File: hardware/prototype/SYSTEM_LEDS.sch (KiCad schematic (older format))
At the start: 9 parts, among them Q1 DTC143Z

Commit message: Complete PCB layout
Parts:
- renumbered D1 to D3, D2 to D4, D19 to D5, D20 to D6, Q1 to Q2, R2 to R8, R6 to R9
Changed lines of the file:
@@
 	1350 4000 1450 4000
 $Comp
-L Device:R R2
+L Device:R R8
 U 1 1 5AE81518
 P 1800 3500
-F 0 "R2" H 1700 3500 50  0000 C CNN
+F 0 "R8" H 1700 3500 50  0000 C CNN
 F 1 "110R" V 1800 3500 50  0000 C CNN
 F 2 "Resistor_SMD:R_0805_2012Metric" V 1730 3500 50  0001 C CNN
@@
 $EndComp
 $Comp
-L power:GND #PWR0101
+L power:GND #PWR041
 U 1 1 5AE8151F
 P 1800 4210
-F 0 "#PWR0101" H 1800 3960 50  0001 C CNN
+F 0 "#PWR041" H 1800 3960 50  0001 C CNN
 F 1 "GND" H 1925 4135 50  0000 C CNN
 F 2 "" H 1800 4210 50  0001 C CNN
@@
 GPS FIX indicator
 $Comp
-L Transistor_BJT:DTC143Z Q1
+L Transistor_BJT:DTC143Z Q2
 U 1 1 5AE81531
 P 1700 4000
-F 0 "Q1" H 1888 4046 50  0000 L CNN
+F 0 "Q2" H 1888 4046 50  0000 L CNN
 F 1 "DTC143Z" H 1888 3955 50  0000 L CNN
 F 2 "Package_TO_SOT_SMD:SC-59_Handsoldering" H 1700 4000 50  0001 L CNN
@@
 	8850 3600 8850 3250
 $Comp
-L power:GND #PWR0102
+L power:GND #PWR043
 U 1 1 5AEBED95
 P 8850 4000
-F 0 "#PWR0102" H 8850 3750 50  0001 C CNN
+F 0 "#PWR043" H 8850 3750 50  0001 C CNN
 F 1 "GND" H 9000 3900 50  0000 C CNN
 F 2 "" H 8850 4000 50  0001 C CNN
@@
 GLOBAL_3V3
 $Comp
-L Device:LED D20
+L Device:LED D6
 U 1 1 5AEBF85D
 P 10650 3100
-F 0 "D20" V 10550 3000 50  0000 R CNN
+F 0 "D6" V 10550 3000 50  0000 R CNN
 F 1 "LED" V 10650 3000 50  0000 R CNN
 F 2 "LED_SMD:LED_0805_2012Metric_Pad0.97x1.50mm_HandSolder" H 10650 3100 50  0001 C CNN
@@
 	10650 3600 10650 3250
 $Comp
-L power:GND #PWR0103
+L power:GND #PWR044
 U 1 1 5AEBF86D
 P 10650 4000
-F 0 "#PWR0103" H 10650 3750 50  0001 C CNN
+F 0 "#PWR044" H 10650 3750 50  0001 C CNN
 F 1 "GND" H 10800 3900 50  0000 C CNN
 F 2 "" H 10650 4000 50  0001 C CNN
@@
 5v power indicator
 $Comp
-L Device:LED D2
+L Device:LED D4
 U 1 1 5AEC051D
 P 5600 3200
-F 0 "D2" V 5550 3100 50  0000 R CNN
+F 0 "D4" V 5550 3100 50  0000 R CNN
 F 1 "LED" V 5650 3100 50  0000 R CNN
 F 2 "LED_SMD:LED_0805_2012Metric_Pad0.97x1.50mm_HandSolder" H 5600 3200 50  0001 C CNN
@@
 	5600 3050 5350 3050
 $Comp
-L Device:R R6
+L Device:R R9
 U 1 1 5AEC0525
 P 5600 3850
-F 0 "R6" H 5700 3850 50  0000 C CNN
+F 0 "R9" H 5700 3850 50  0000 C CNN
 F 1 "130R" V 5600 3850 50  0000 C CNN
 F 2 "Resistor_SMD:R_0805_2012Metric" V 5530 3850 50  0001 C CNN
@@
 	5600 3700 5600 3350
 $Comp
-L power:GND #PWR0104
+L power:GND #PWR042
 U 1 1 5AEC052D
 P 5600 4100
-F 0 "#PWR0104" H 5600 3850 50  0001 C CNN
+F 0 "#PWR042" H 5600 3850 50  0001 C CNN
 F 1 "GND" H 5750 4000 50  0000 C CNN
 F 2 "" H 5600 4100 50  0001 C CNN
@@
 Red_LED
 $Comp
-L Device:LED D19
+L Device:LED D5
 U 1 1 5AEC1D57
 P 8850 3100
-F 0 "D19" V 8750 3000 50  0000 R CNN
+F 0 "D5" V 8750 3000 50  0000 R CNN
 F 1 "LED" V 8850 3000 50  0000 R CNN
 F 2 "LED_SMD:LED_0805_2012Metric_Pad0.97x1.50mm_HandSolder" H 8850 3100 50  0001 C CNN
@@
 $EndComp
 $Comp
-L Device:LED D1
+L Device:LED D3
 U 1 1 5B00BAB6
 P 1800 3100
-F 0 "D1" V 1700 3000 50  0000 R CNN
+F 0 "D3" V 1700 3000 50  0000 R CNN
 F 1 "LED" V 1800 3000 50  0000 R CNN
 F 2 "LED_SMD:LED_0805_2012Metric_Pad0.97x1.50mm_HandSolder" H 1800 3100 50  0001 C CNN

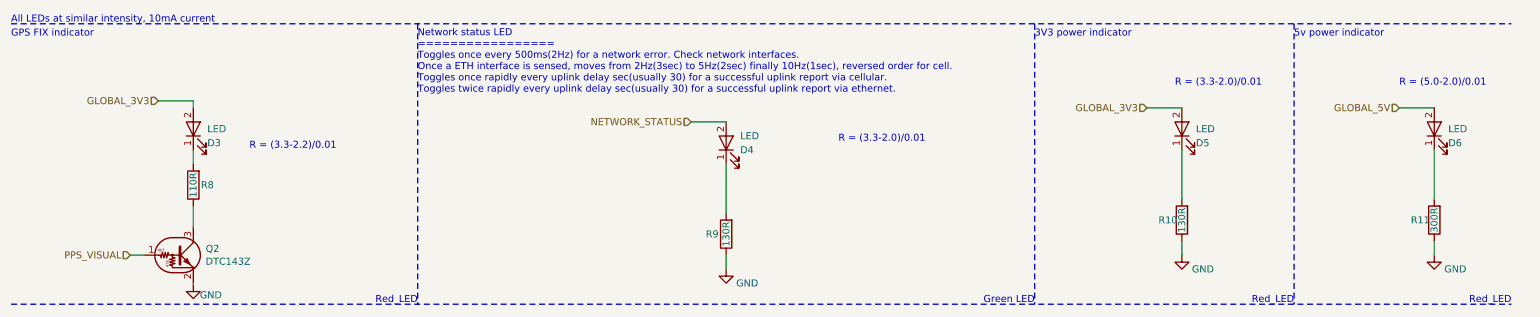
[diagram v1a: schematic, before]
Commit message: Complete PCB design, BOM generation and gerber generation
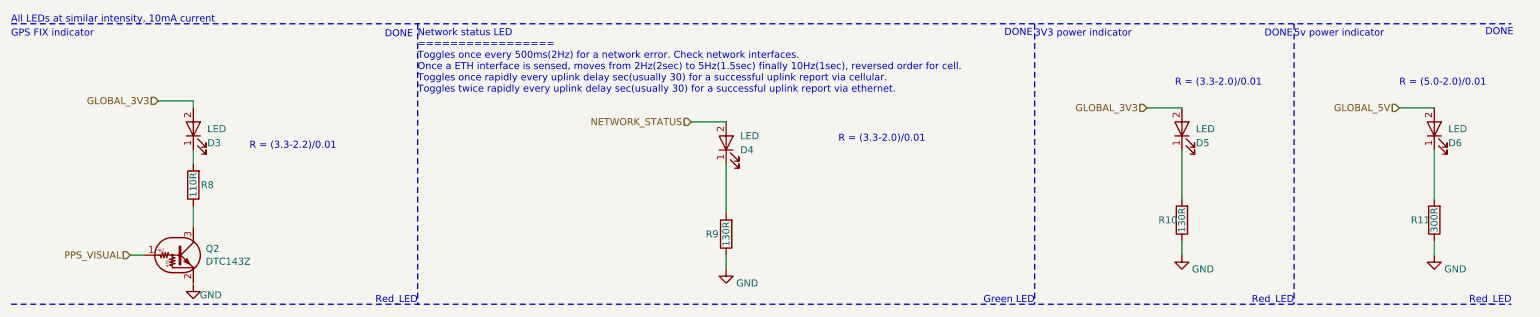
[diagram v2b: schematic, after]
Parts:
- D3, D5, D6: manf# (none) -> LTST-C171KRKT
- D4: manf# (none) -> LTST-C171KGKT
- Q2: manf# (none) -> DTC143ZKAT146
- R10, R9: manf# (none) -> ERA-6AEB131V; purchase_page (none) -> https://www.digikey.com/product-detail/en/panasonic-electro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
- R11: manf# (none) -> ERJ-PB6D3000V; purchase_page (none) -> https://www.digikey.com/product-detail/en/panasonic-electro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
- R8: manf# (none) -> CRCW0805110RFKEA; purchase_page (none) -> https://www.digikey.com/product-detail/en/vishay-dale/CRCW0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
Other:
- note added: "DONE"
- note added: "Network status LED\n=================\nToggles once every 500ms(2Hz) for a network error. Check network interfaces.\nOnce a ETH interface is sensed, moves from 2Hz(2sec) to 5Hz(1.5sec) finally 10Hz(1sec), reversed order for cell.\nToggles once rapidly every uplink delay sec(usually 30) for a successful uplink report via cellular.\nToggles twice rapidly every uplink delay sec(usually 30) for a suc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"
- note removed: "Network status LED\n=================\nToggles once every 500ms(2Hz) for a network error. Check network interfaces.\nOnce a ETH interface is sensed, moves from 2Hz(3sec) to 5Hz(2sec) finally 10Hz(1sec), reversed order for cell.\nToggles once rapidly every uplink delay sec(usually 30) for a successful uplink report via cellular.\nToggles twice rapidly every uplink delay sec(usually 30) for a succe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"
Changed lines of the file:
@@
 $Descr A4 11693 8268
 encoding utf-8
-Sheet 2 2
-Title ""
-Date ""
-Rev ""
-Comp ""
-Comment1 ""
+Sheet 2 3
+Title "ESP32 LoRa gateway with surge suppression"
+Date "2018-04-30"
+Rev "1"
+Comp "Kaiote Limited"
+Comment1 "Design by: Alois Mbutura"
 Comment2 ""
 Comment3 ""
@@
 F 1 "110R" V 1800 3500 50  0000 C CNN
 F 2 "Resistor_SMD:R_0805_2012Metric" V 1730 3500 50  0001 C CNN
-F 3 "~" H 1800 3500 50  0001 C CNN
+F 3 "http://www.vishay.com/docs/20035/dcrcwe3.pdf" H 1800 3500 50  0001 C CNN
+F 4 "https://www.digikey.com/product-detail/en/vishay-dale/CRCW0805110RFKEA/541-110CCT-ND/1180673" H 1800 3500 50  0001 C CNN "purchase_page"
+F 5 "CRCW0805110RFKEA" H 1800 3500 50  0001 C CNN "manf#"
 	1    1800 3500
 	-1   0    0    1
@@
 F 3 "http://www.rohm.com/web/global/datasheet/DTC143ZEB/dtc143zebtl-e" H 1700 4000 50  0001 L CNN
 F 4 "https://www.digikey.com/product-detail/en/rohm-semiconductor/DTC143ZKAT146/DTC143ZKAT146CT-ND/650725" H 1700 4000 50  0001 C CNN "purchase page"
+F 5 "DTC143ZKAT146" H 1700 4000 50  0001 C CNN "manf#"
 	1    1700 4000
 	1    0    0    -1
@@
 GLOBAL_3V3
 Text Notes 3400 2850 0    50   ~ 0
-Network status LED\n=================\nToggles once every 500ms(2Hz) for a network error. Check network interfaces.\nOnce a ETH interface is sensed, moves from 2Hz(3sec) to 5Hz(2sec) finally 10Hz(1sec), reversed order for cell.\nToggles once rapidly every uplink delay sec(usually 30) for a successful uplink report via cellular.\nToggles twice rapidly every uplink delay sec(usually 30) for a successful uplink report via ethernet.
+Network status LED\n=================\nToggles once every 500ms(2Hz) for a network error. Check network interfaces.\nOnce a ETH interface is sensed, moves from 2Hz(2sec) to 5Hz(1.5sec) finally 10Hz(1sec), reversed order for cell.\nToggles once rapidly every uplink delay sec(usually 30) for a successful uplink report via cellular.\nToggles twice rapidly every uplink delay sec(usually 30) for a successful uplink report via ethernet.
 Wire Notes Line
 	3400 2350 3400 4350
@@
 F 3 "http://optoelectronics.liteon.com/upload/download/DS22-2000-109/LTST-C171KRKT.pdf" H 10650 3100 50  0001 C CNN
 F 4 "https://www.digikey.com/product-detail/en/lite-on-inc/LTST-C171KRKT/160-1427-1-ND/386800" H 10650 3100 50  0001 C CNN "purchase page"
+F 5 "LTST-C171KRKT" V 10650 3100 50  0001 C CNN "manf#"
 	1    10650 3100
 	0    -1   -1   0
@@
 F 1 "300R" V 10650 3750 50  0000 C CNN
 F 2 "Resistor_SMD:R_0805_2012Metric" V 10580 3750 50  0001 C CNN
-F 3 "~" H 10650 3750 50  0001 C CNN
+F 3 "https://industrial.panasonic.com/cdbs/www-data/pdf/RDM0000/AOA0000C328.pdf" H 10650 3750 50  0001 C CNN
+F 4 "ERJ-PB6D3000V" H 10650 3750 50  0001 C CNN "manf#"
+F 5 "https://www.digikey.com/product-detail/en/panasonic-electronic-components/ERJ-PB6D3000V/P20957CT-ND/6215212" H 10650 3750 50  0001 C CNN "purchase_page"
 	1    10650 3750
 	-1   0    0    1
@@
 F 3 "http://optoelectronics.liteon.com/upload/download/DS22-2000-118/LTST-C171KGKT.pdf" H 5600 3200 50  0001 C CNN
 F 4 "https://www.digikey.com/product-detail/en/lite-on-inc/LTST-C171KGKT/160-1426-1-ND/386798" H 5600 3200 50  0001 C CNN "purchase page"
+F 5 "LTST-C171KGKT " V 5600 3200 50  0001 C CNN "manf#"
 	1    5600 3200
 	0    -1   -1   0
@@
 F 1 "130R" V 5600 3850 50  0000 C CNN
 F 2 "Resistor_SMD:R_0805_2012Metric" V 5530 3850 50  0001 C CNN
-F 3 "~" H 5600 3850 50  0001 C CNN
+F 3 "https://industrial.panasonic.com/cdbs/www-data/pdf/RDM0000/AOA0000C307.pdf" H 5600 3850 50  0001 C CNN
+F 4 "https://www.digikey.com/product-detail/en/panasonic-electronic-components/ERA-6AEB131V/P130DACT-ND/1465926" H 5600 3850 50  0001 C CNN "purchase_page"
+F 5 "ERA-6AEB131V" H 5600 3850 50  0001 C CNN "manf#"
 	1    5600 3850
 	-1   0    0    1
@@
 F 3 "http://optoelectronics.liteon.com/upload/download/DS22-2000-109/LTST-C171KRKT.pdf" H 8850 3100 50  0001 C CNN
 F 4 "https://www.digikey.com/product-detail/en/lite-on-inc/LTST-C171KRKT/160-1427-1-ND/386800" H 8850 3100 50  0001 C CNN "purchase page"
+F 5 "LTST-C171KRKT" V 8850 3100 50  0001 C CNN "manf#"
 	1    8850 3100
 	0    -1   -1   0
@@
 F 3 "http://optoelectronics.liteon.com/upload/download/DS22-2000-109/LTST-C171KRKT.pdf" H 1800 3100 50  0001 C CNN
 F 4 "https://www.digikey.com/product-detail/en/lite-on-inc/LTST-C171KRKT/160-1427-1-ND/386800" H 1800 3100 50  0001 C CNN "purchase page"
+F 5 "LTST-C171KRKT" V 1800 3100 50  0001 C CNN "manf#"
 	1    1800 3100
 	0    -1   -1   0
@@
 F 1 "130R" V 8850 3750 50  0000 C CNN
 F 2 "Resistor_SMD:R_0805_2012Metric" V 8780 3750 50  0001 C CNN
-F 3 "~" H 8850 3750 50  0001 C CNN
+F 3 "https://industrial.panasonic.com/cdbs/www-data/pdf/RDM0000/AOA0000C307.pdf" H 8850 3750 50  0001 C CNN
+F 4 "ERA-6AEB131V" H 8850 3750 50  0001 C CNN "manf#"
+F 5 "https://www.digikey.com/product-detail/en/panasonic-electronic-components/ERA-6AEB131V/P130DACT-ND/1465926" H 8850 3750 50  0001 C CNN "purchase_page"
 	1    8850 3750
 	-1   0    0    1
@@
 Text Notes 10400 2800 0    50   ~ 0
 R = (5.0-2.0)/0.01
+Text Notes 3165 2455 0    50   ~ 0
+DONE
+Text Notes 7785 2445 2    50   ~ 0
+DONE
+Text Notes 9640 2450 2    50   ~ 0
+DONE
+Text Notes 11215 2440 2    50   ~ 0
+DONE
 $EndSCHEMATC
